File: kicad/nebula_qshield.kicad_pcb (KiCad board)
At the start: 4 copper layers, 100 x 100 mm, 153 parts, among them J1 J1, J10 J10, J11 J11, J12 J12, J13 J13, J14 J14, J15 J15, J16 J16, J17 J17, J18 J18, J19 J19, J2 J2, J20 J20, J21 J21, J3 J3, J4 J4, J5 J5, J6 J6, J7 J7, J8 J8, J9 J9, K1 HF46F-12-HS1, K2 HF46F-12-HS1, Q1 IRLZ44NPBF, Q2 IRLZ44NPBF, Q3 2N7002, Q4 2N7002, Q5 IRLZ44NPBF, SW1 RESET, T1 Transformer_SP_2S, T2 Transformer_SP_2S, T3 Transformer_SP_2S, U1 TPS54302DDCR, U10 MCP6002, U11 MCP6002, U12 SN6501, U13 AMC1301, U14 HX711, U15 MAX485ESA, U16 PC817X2NIP, U17 IR2104SPBF, U18 PC817X1NIP, U19 PC817X1NIP, U2 AMS1117-3.3, U20 MCP6002, U21 ISO1541, U3 TPS3823-33DBVR, U4 MCP6002, U5 SN6501, U6 AMC1301, U7 MCP6002, U8 SN6501, U9 AMC1301

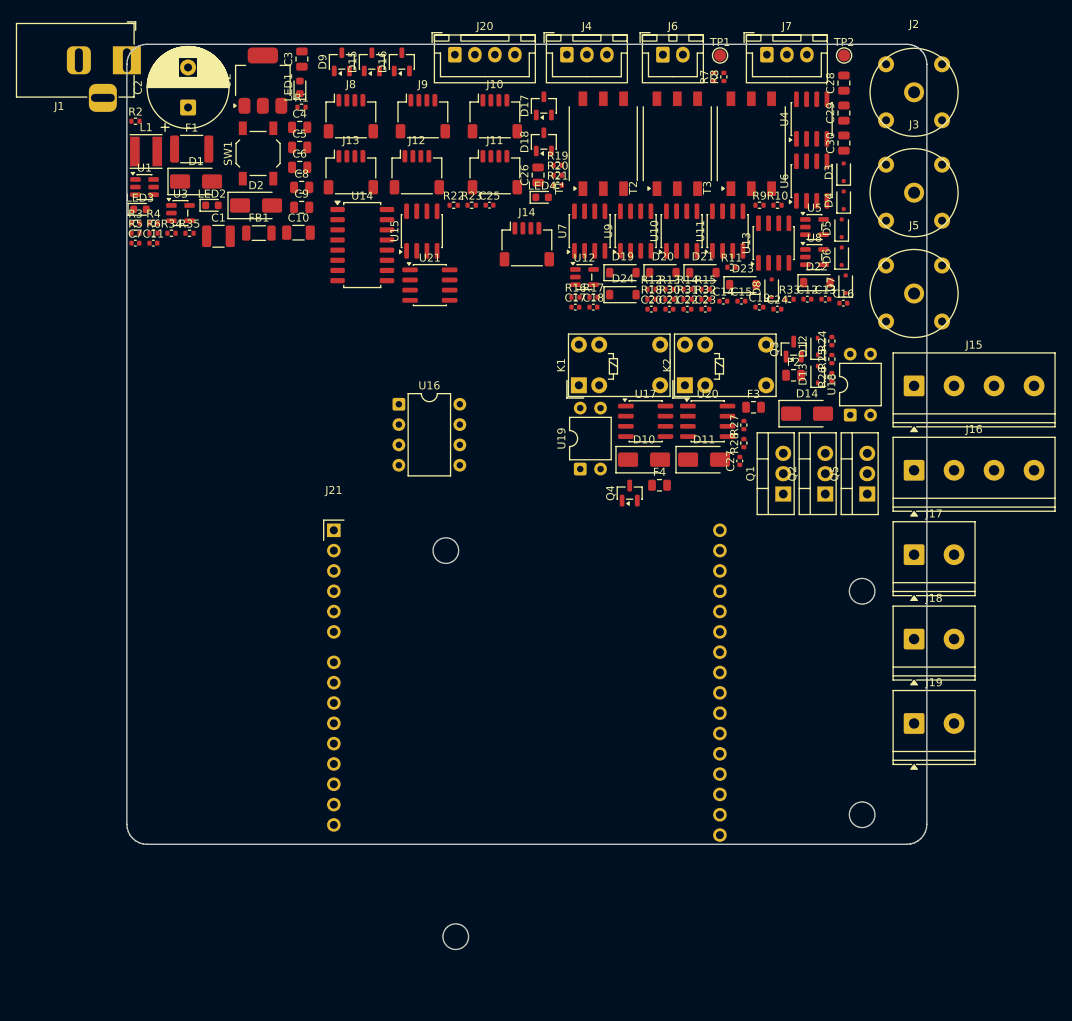
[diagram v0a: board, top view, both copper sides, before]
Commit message: feat(routing): initial autoroute and copper DRC baseline
Co-Authored-By: Devin AI <158243242+devin-ai-integration[bot]@users.noreply.github.com>
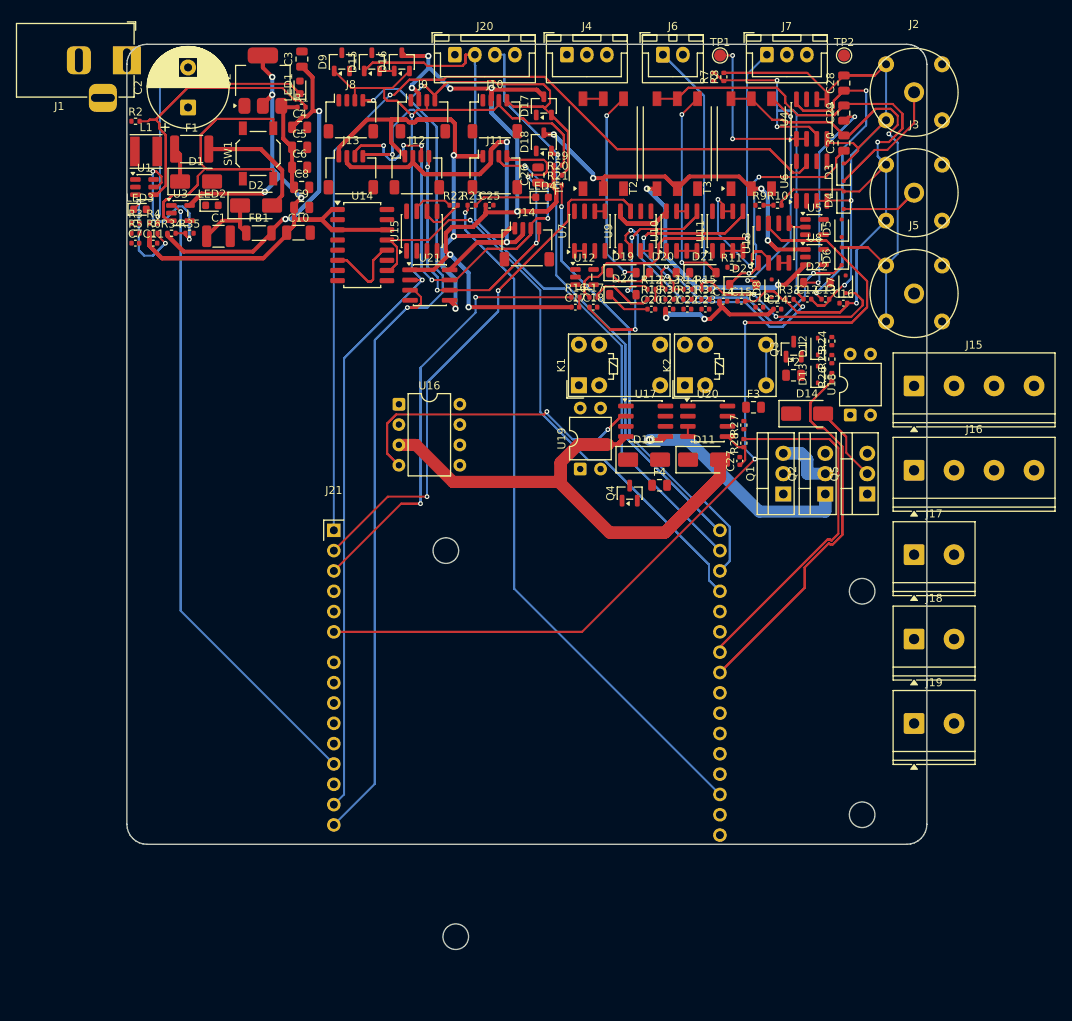
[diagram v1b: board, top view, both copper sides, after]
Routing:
- net /3V3_RAIL: track 0.00 -> 278.5 mm, vias 0 -> 13
- net /I2C_SCL: track 0.00 -> 275.5 mm, vias 0 -> 3
- net /I2C_SDA: track 0.00 -> 253.3 mm, vias 0 -> 2
- net /DO_ADC: track 0.00 -> 195.3 mm, vias 0 -> 2
- net /PH_ADC: track 0.00 -> 174.2 mm, vias 0 -> 1
- net /HMI_TX: track 0.00 -> 172.9 mm
- net /Analog Acquisition/GND_ISO_ORP: track 0.00 -> 154.0 mm, vias 0 -> 2
- net /LED_STATUS: track 0.00 -> 136.9 mm, vias 0 -> 1
- net /HMI_RX: track 0.00 -> 129.8 mm, vias 0 -> 1
- net /MCU_NRST: track 0.00 -> 128.4 mm, vias 0 -> 1
- net /HX711_DOUT: track 0.00 -> 122.7 mm, vias 0 -> 1
- net /Digital & I2C/SCL_ISO: track 0.00 -> 121.3 mm, vias 0 -> 5
- net /HX711_SCK: track 0.00 -> 117.2 mm, vias 0 -> 1
- net /PGND: track 0.00 -> 112.5 mm
- net /Analog Acquisition/GND_ISO_PH: track 0.00 -> 107.0 mm, vias 0 -> 2
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
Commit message: feat(routing): manual DRC cleanup and additional autorouting pass
Co-Authored-By: Devin AI <158243242+devin-ai-integration[bot]@users.noreply.github.com>
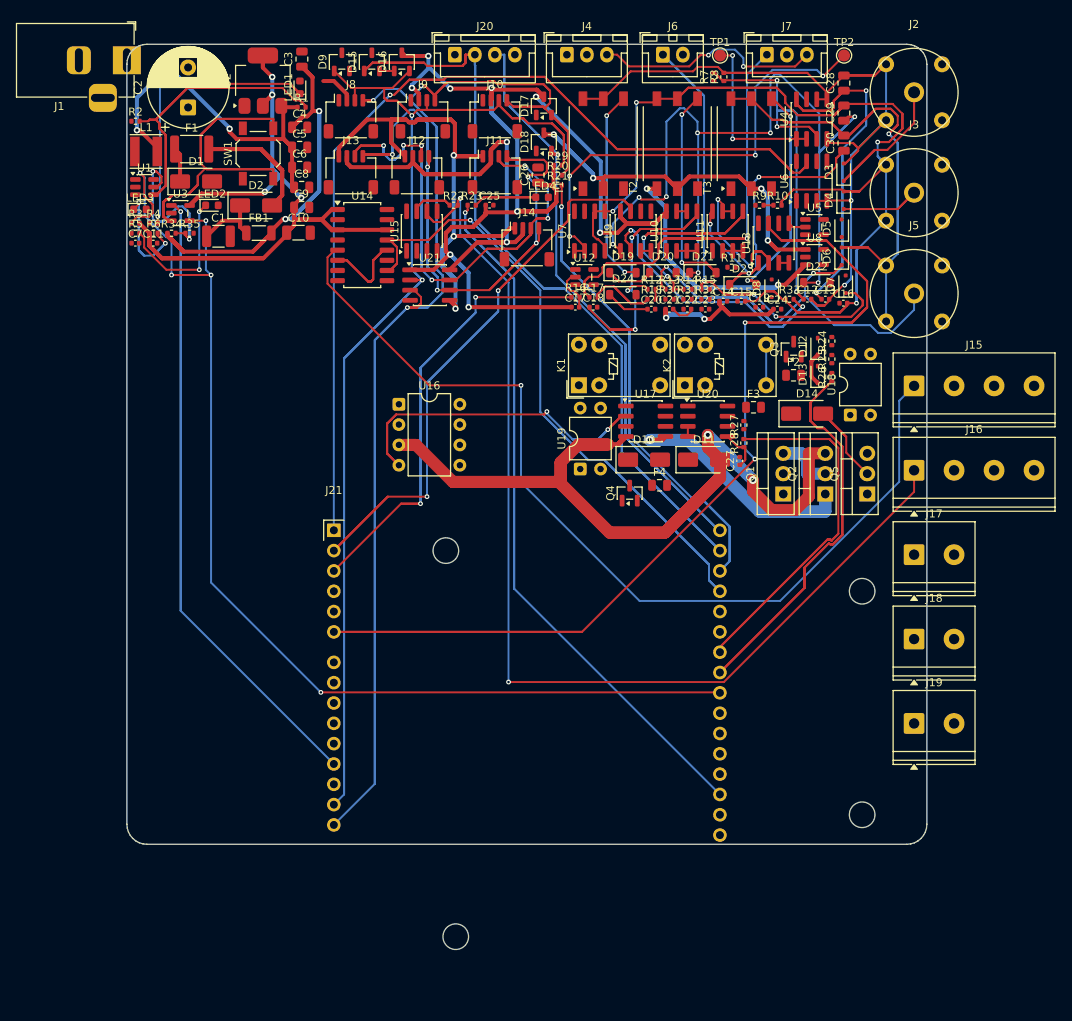
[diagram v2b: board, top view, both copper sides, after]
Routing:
- net /MCU_WDI: track 0.00 -> 145.1 mm, vias 0 -> 5
- net /Digital & I2C/RS485_A: track 10.2 -> 138.6 mm, vias 0 -> 2
- net /Digital & I2C/HX711_EP: track 0.00 -> 118.8 mm, vias 0 -> 1
- net /Analog Acquisition/VDD_ISO_ORP: track 33.3 -> 109.2 mm, vias 2 -> 8
- net /Analog Acquisition/ORP_BUF: track 1.27 -> 57.9 mm, vias 0 -> 4
- net /3V3_RAIL: track 278.5 -> 315.0 mm, vias 13 -> 15
- net /Analog Acquisition/DO_SIG: track 60.2 -> 93.9 mm
- net /5V_RAIL: track 80.9 -> 113.9 mm, vias 4 -> 6
- net /PGND: track 112.5 -> 141.8 mm, vias 0 -> 2
- net /AGND: track 0.00 -> 28.6 mm, vias 0 -> 2
- net /Analog Acquisition/GND_ISO_ORP: track 154.0 -> 182.0 mm, vias 2 -> 4
- net /Analog Acquisition/DO_SEC_A: track 31.2 -> 53.8 mm
- net /HMI_TX: track 172.9 -> 192.8 mm
- net Net-(LED2-K): track 0.00 -> 18.5 mm, vias 0 -> 2
- net /Power Management/VIN: track 66.5 -> 84.6 mm
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
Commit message: feat(routing): safe GND via and zone baseline for remaining unconnected items
- Add tools/route_gnd_manual.py: resets GND zones to full/z-clearance,
  removes stubs, recreates GND vias with F.Cu/B.Cu pads, and drops vias
  on SMD GND pads clear of B.Cu obstacles.
- Apply to kicad/nebula_qshield.kicad_pcb:
  * unconnected_items: 181 -> 132
  * no new clearance/shorting/tracks_crossing copper violations
  * replaces one pre-existing track_dangling warning with one
    isolated_copper warning in a 3V3_RAIL In2.Cu zone (pending manual
    3V3 routing in a follow-up PR).

Manual F.Cu tracks for the remaining GND clusters will be handled in the
next PR.

Co-Authored-By: Devin AI <158243242+devin-ai-integration[bot]@users.noreply.github.com>
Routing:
- net /3V3_RAIL: track 315.0 -> 311.3 mm
- net GND: vias 0 -> 35
- added copper zone on B.Cu, net GND

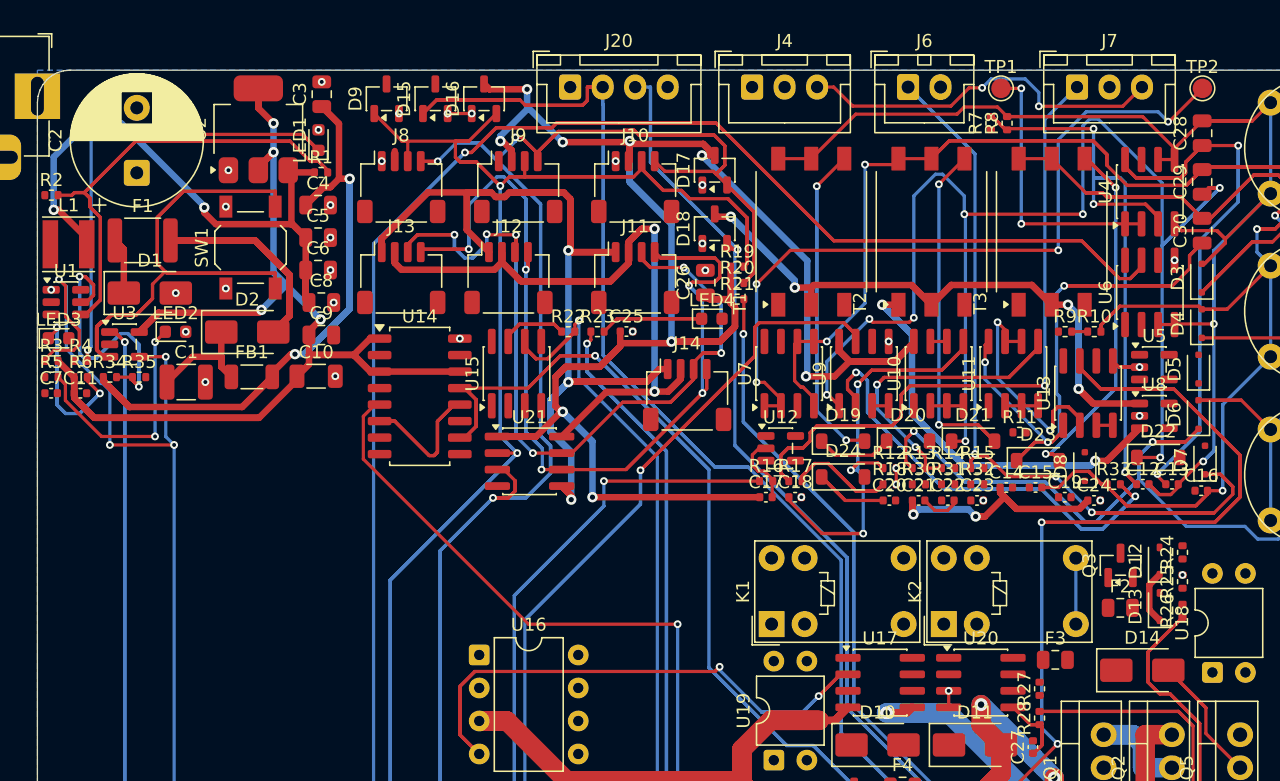
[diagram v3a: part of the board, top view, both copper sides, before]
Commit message: feat(routing): manual GND via routing for U3/R35/C11 clusters and EN_UVLO detour
- Reroute /Power Management/EN_UVLO on B.Cu and F.Cu to clear the U3 and
  R35 GND pads, keeping a safe clearance from MCU_NRST and MCU_WDI.
- Replace and add 0.6/0.3 mm GND vias with per-net clearance, lowering
  unconnected_items from 132 to 123.
- DRC copper violations unchanged (no new clearance/shorting/tracks_crossing
  items).

Co-Authored-By: Devin AI <158243242+devin-ai-integration[bot]@users.noreply.github.com>
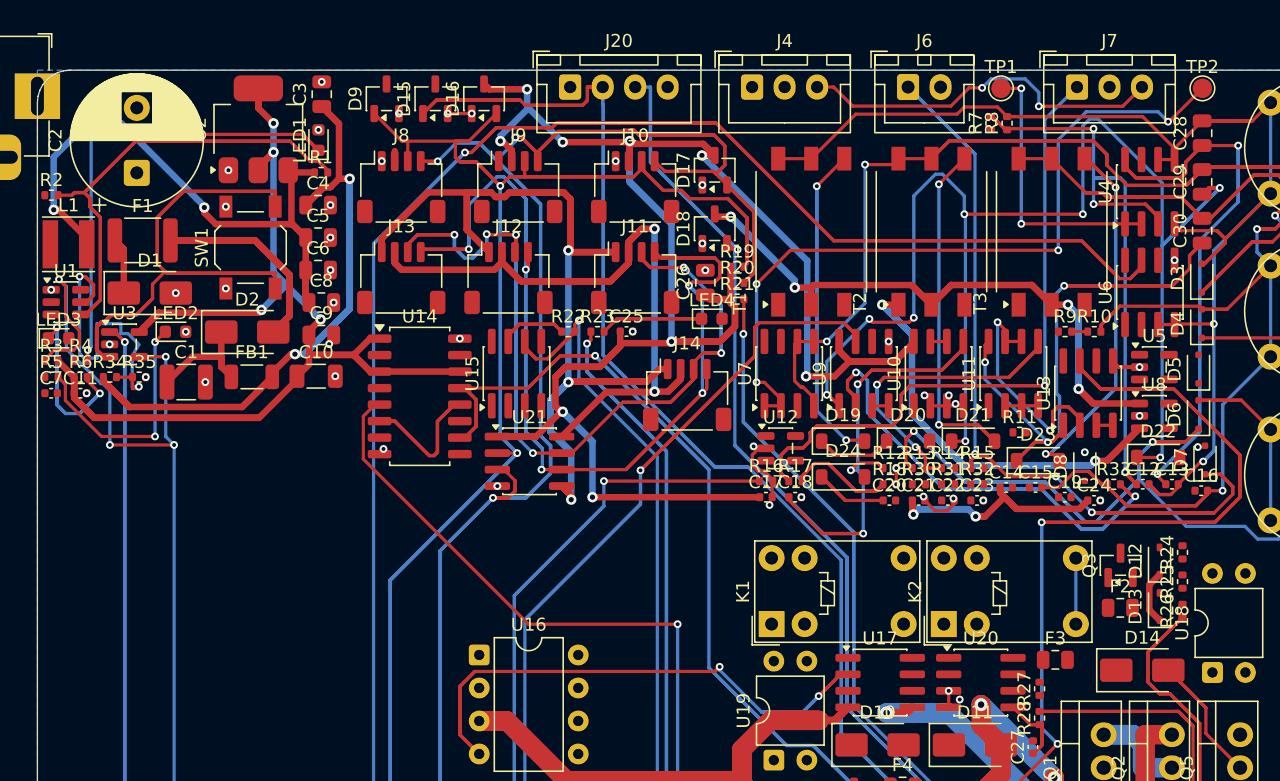
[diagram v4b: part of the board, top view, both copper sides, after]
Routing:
- net /Power Management/EN_UVLO: track 39.6 -> 27.4 mm
- net GND: vias 35 -> 50

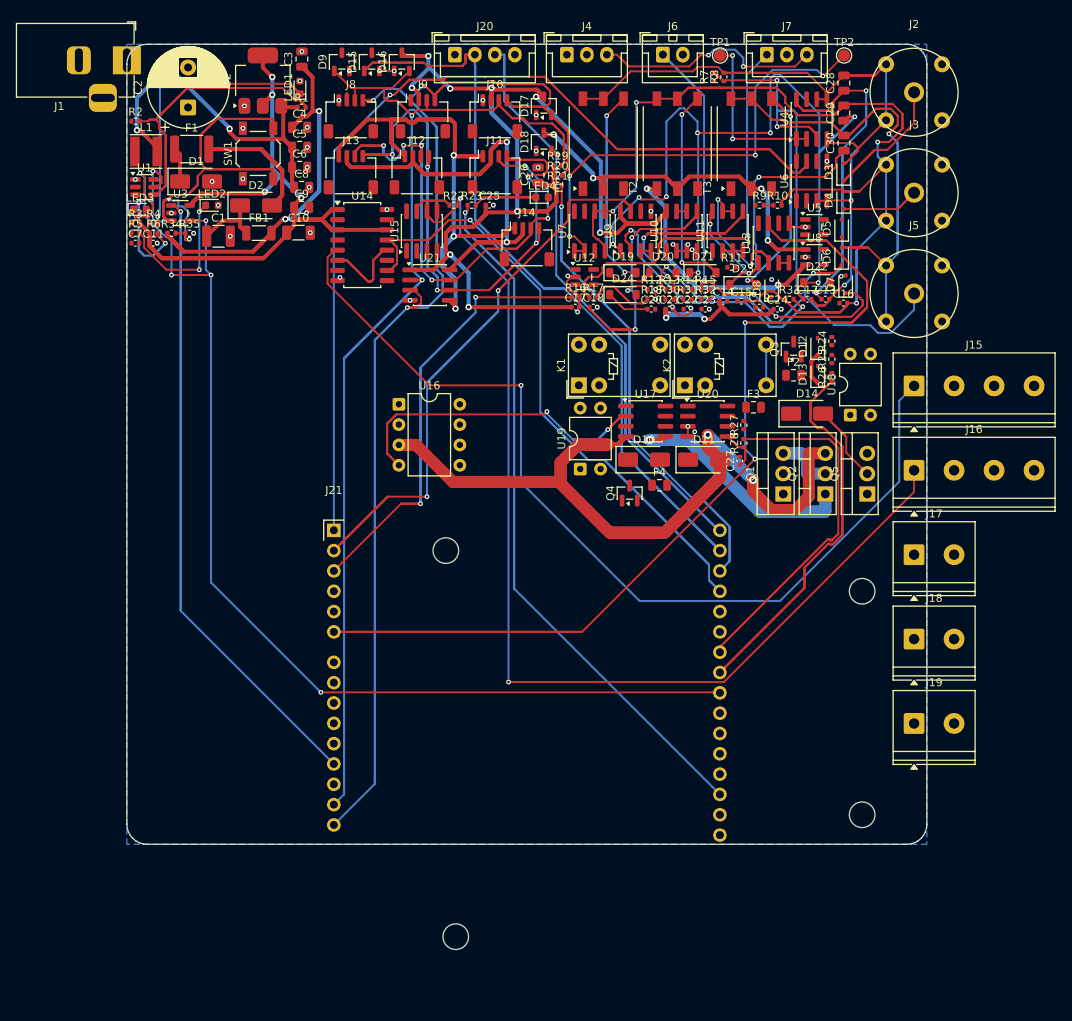
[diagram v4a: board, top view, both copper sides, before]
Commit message: feat(routing): FreeRouting pase completo v1.7 (mp=10): 0 DRC violations
FreeRouting pase completo v1.7 (mp=10): 0 DRC violations

Status:
  - Antes: 123 unconnected
  - Después: 103 unconnected (-20 items)
  - DRC violations: 0
  - Routing: mixed (Zona A + partial Zona B/C)

Próxima fase: análisis específico de Zona A routing
para validar que power/ground/feedback cumplen specs.

Co-Authored-By: Devin AI <158243242+devin-ai-integration[bot]@users.noreply.github.com>
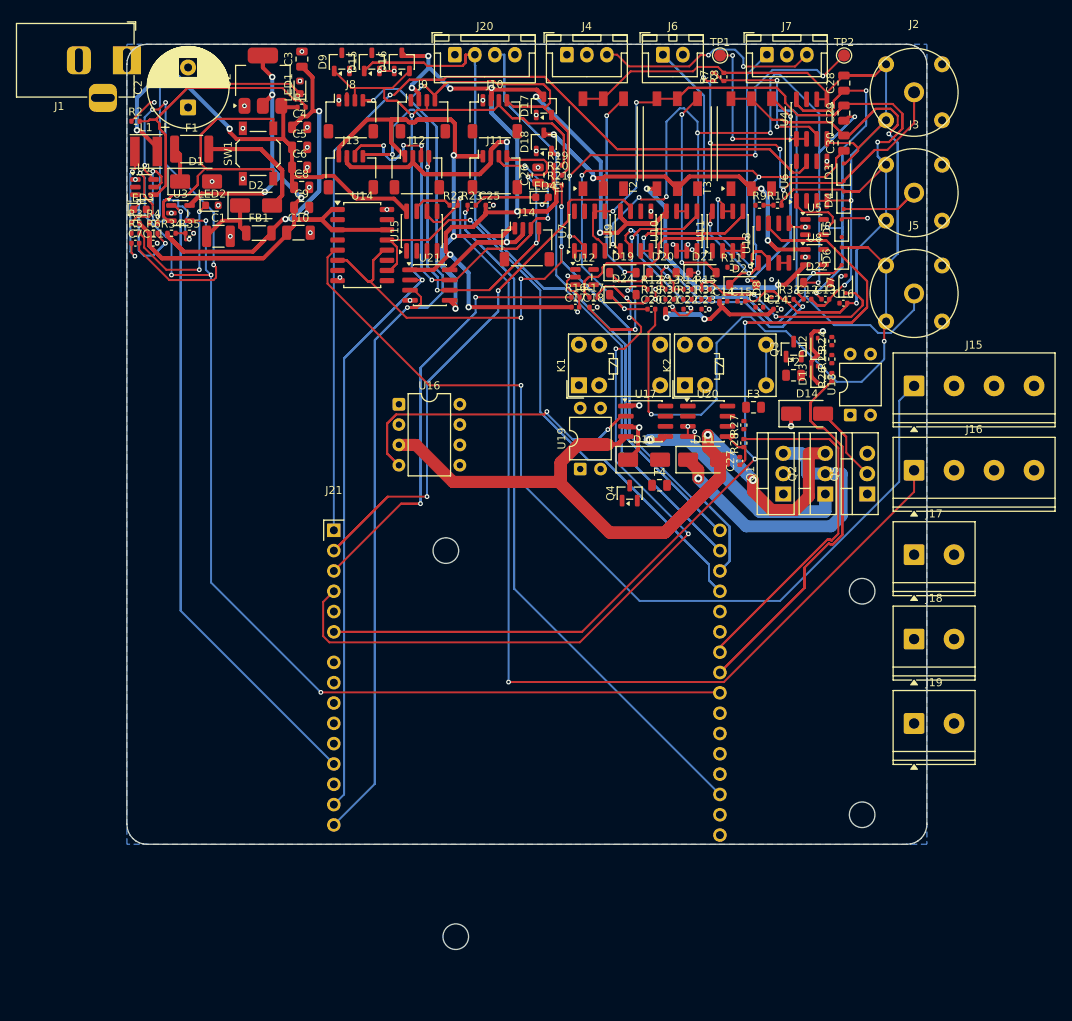
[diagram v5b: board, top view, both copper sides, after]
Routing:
- net /HUM_ADC: track 15.5 -> 109.7 mm, vias 0 -> 4
- net /Analog Acquisition/GND_ISO_DO: track 102.5 -> 163.8 mm, vias 1 -> 3
- net Net-(U1-BOOT): track 0.00 -> 48.3 mm, vias 0 -> 4
- net /Analog Acquisition/VDD_ISO_DO: track 70.0 -> 111.6 mm, vias 3 -> 5
- net /HX711_DOUT: track 134.9 -> 168.3 mm, vias 1 -> 4
- net /Analog Acquisition/PH_SIG: track 32.1 -> 64.4 mm, vias 0 -> 4
- net /Actuator Drivers/MOTOR_VS: track 12.5 -> 43.6 mm, vias 0 -> 1
- net /5V_RAIL: track 113.9 -> 130.1 mm
- net /Power Management/SW: track 0.00 -> 15.4 mm, vias 0 -> 2
- net /12V_RAIL: track 14.4 -> 28.5 mm, vias 0 -> 4
- net GND: track 19.3 -> 30.6 mm, vias 50 -> 53
- net /Analog Acquisition/VDD_ISO_PH: track 81.2 -> 90.4 mm, vias 2 -> 3
- net Net-(U3-~{MR}): track 96.0 -> 90.6 mm
- net /PGND: track 141.8 -> 147.0 mm
- net /3V3_RAIL: track 311.3 -> 315.0 mm
